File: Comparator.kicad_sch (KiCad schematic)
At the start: 15 parts, among them U501 AZV3002S-13

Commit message: fix: test point changes
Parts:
- TP501, TP502: footprint TestPoint:TestPoint_Pad_D1.5mm -> TestPoint:TestPoint_Pad_D1.0mm
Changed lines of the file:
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@@
 			)
 		)
-		(property "Footprint" "TestPoint:TestPoint_Pad_D1.5mm"
+		(property "Footprint" "TestPoint:TestPoint_Pad_D1.0mm"
 			(at 87.63 66.04 0)
 			(effects
@@
 			)
 		)
-		(property "Datasheet" "~"
+		(property "Datasheet" ""
 			(at 87.63 66.04 0)
 			(effects
@@
 			)
 		)
-		(property "Description" "test point"
+		(property "Description" ""
 			(at 92.71 66.04 0)
 			(effects
@@
 			)
 		)
-		(property "Footprint" "TestPoint:TestPoint_Pad_D1.5mm"
+		(property "Footprint" "TestPoint:TestPoint_Pad_D1.0mm"
 			(at 151.13 66.04 0)
 			(effects
@@
 			)
 		)
-		(property "Datasheet" "~"
+		(property "Datasheet" ""
 			(at 151.13 66.04 0)
 			(effects
@@
 			)
 		)
-		(property "Description" "test point"
+		(property "Description" ""
 			(at 156.21 66.04 0)
 			(effects

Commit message: fix: bom improvements & more notes
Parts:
- D501, D502: Notes (none) -> Fast switching diode, low leakage, used for diode-AND logic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
- TP501, TP502: footprint TestPoint:TestPoint_Pad_D1.0mm -> RD-Testpoints:TestPoint_Pad_D1.0mm
- TP503: footprint TestPoint:TestPoint_Pad_D1.5mm -> RD-Testpoints:TestPoint_Pad_D1.5mm
- U501: Notes (none) -> Dual comparator, low supply current, wide supply voltage ra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
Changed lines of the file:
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@@
 			)
 		)
-		(property "Footprint" "TestPoint:TestPoint_Pad_D1.0mm"
+		(property "Footprint" "RD-Testpoints:TestPoint_Pad_D1.0mm"
 			(at 87.63 66.04 0)
 			(effects
@@
 			)
 		)
-		(property "Footprint" "TestPoint:TestPoint_Pad_D1.5mm"
+		(property "Footprint" "RD-Testpoints:TestPoint_Pad_D1.5mm"
 			(at 208.28 72.39 0)
 			(effects
@@
 			)
 		)
+		(property "Notes" "Dual comparator, low supply current, wide supply voltage range, suitable for voltage threshold detection"
+			(at 130.81 66.04 0)
+			(effects
+				(font
+					(size 1.27 1.27)
+				)
+				(hide yes)
+			)
+		)
 		(pin "6"
 		)
@@
 			)
 		)
-		(property "Footprint" "TestPoint:TestPoint_Pad_D1.0mm"
+		(property "Footprint" "RD-Testpoints:TestPoint_Pad_D1.0mm"
 			(at 151.13 66.04 0)
 			(effects
@@
 			)
 		)
+		(property "Notes" "Fast switching diode, low leakage, used for diode-AND logic gating of control signals"
+			(at 195.58 85.09 0)
+			(effects
+				(font
+					(size 1.27 1.27)
+				)
+				(hide yes)
+			)
+		)
 		(pin "1"
 		)
@@
 				)
 				(justify left top)
+				(hide yes)
+			)
+		)
+		(property "Notes" "Dual comparator, low supply current, wide supply voltage range, suitable for voltage threshold detection"
+			(at 67.31 66.04 0)
+			(effects
+				(font
+					(size 1.27 1.27)
+				)
 				(hide yes)
 			)
@@
 			(at 195.58 72.39 0)
 			(effects
+				(font
+					(size 1.27 1.27)
+				)
+				(hide yes)
+			)
+		)
+		(property "Notes" "Fast switching diode, low leakage, used for diode-AND logic gating of control signals"
+			(at 195.58 72.39 0)
+			(effects

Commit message: feat: ERC/DRC checks
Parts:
- R501, R502, R503, R504, R505, R506, R507: Manufacturer (none) -> Analog Technologies
- U501: footprint Package_SO:Diodes_SO-8EP -> AZV3002S-13:Diodes_SO-8EP

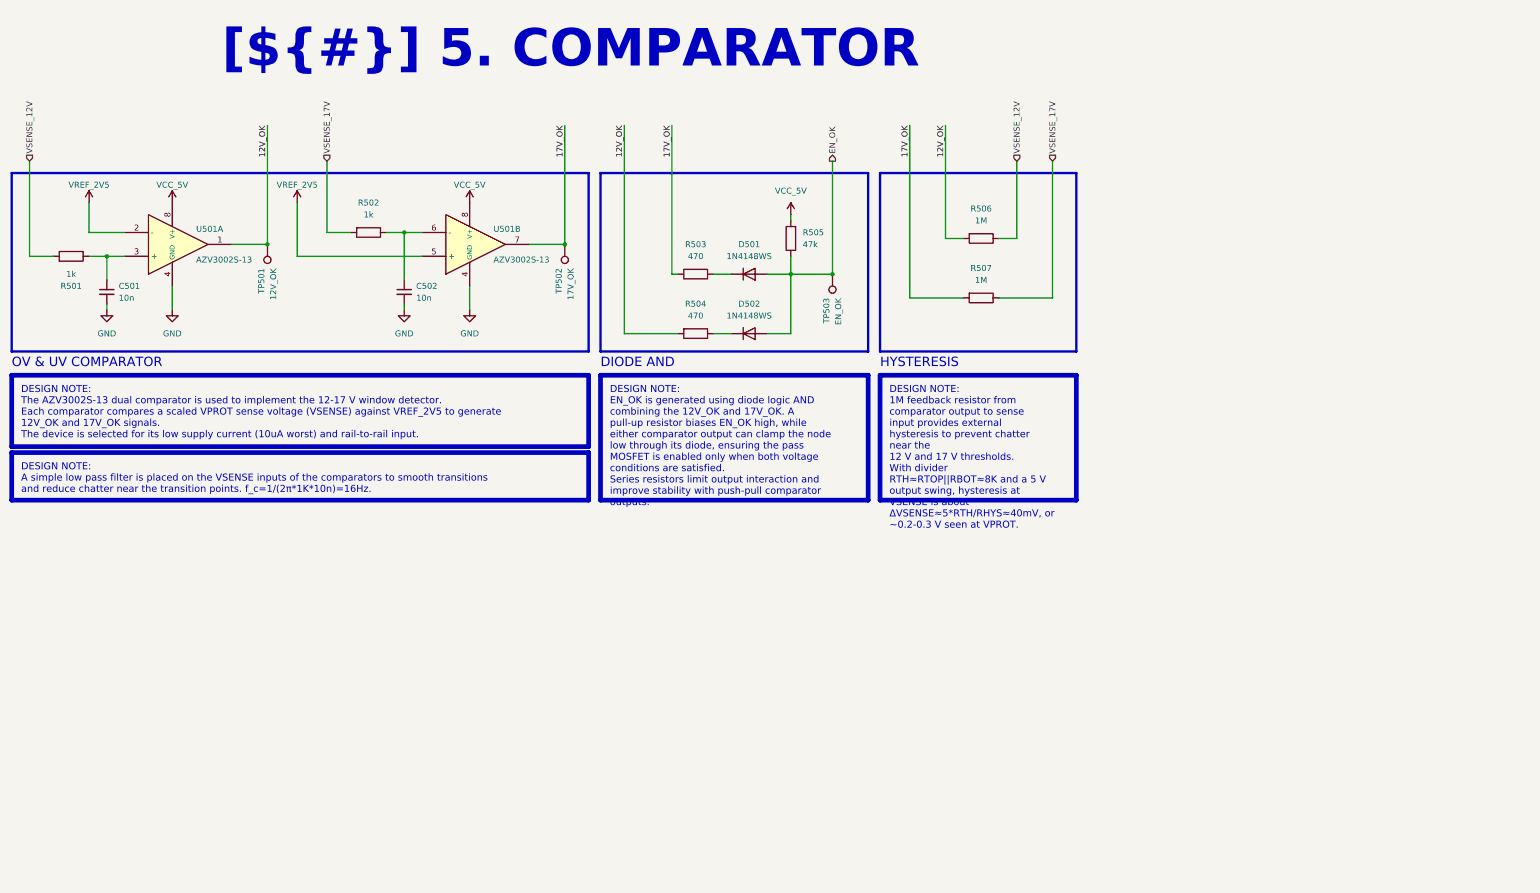
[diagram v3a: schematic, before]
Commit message: feat!: added OC protection, redesigned board from near scratch, size increase
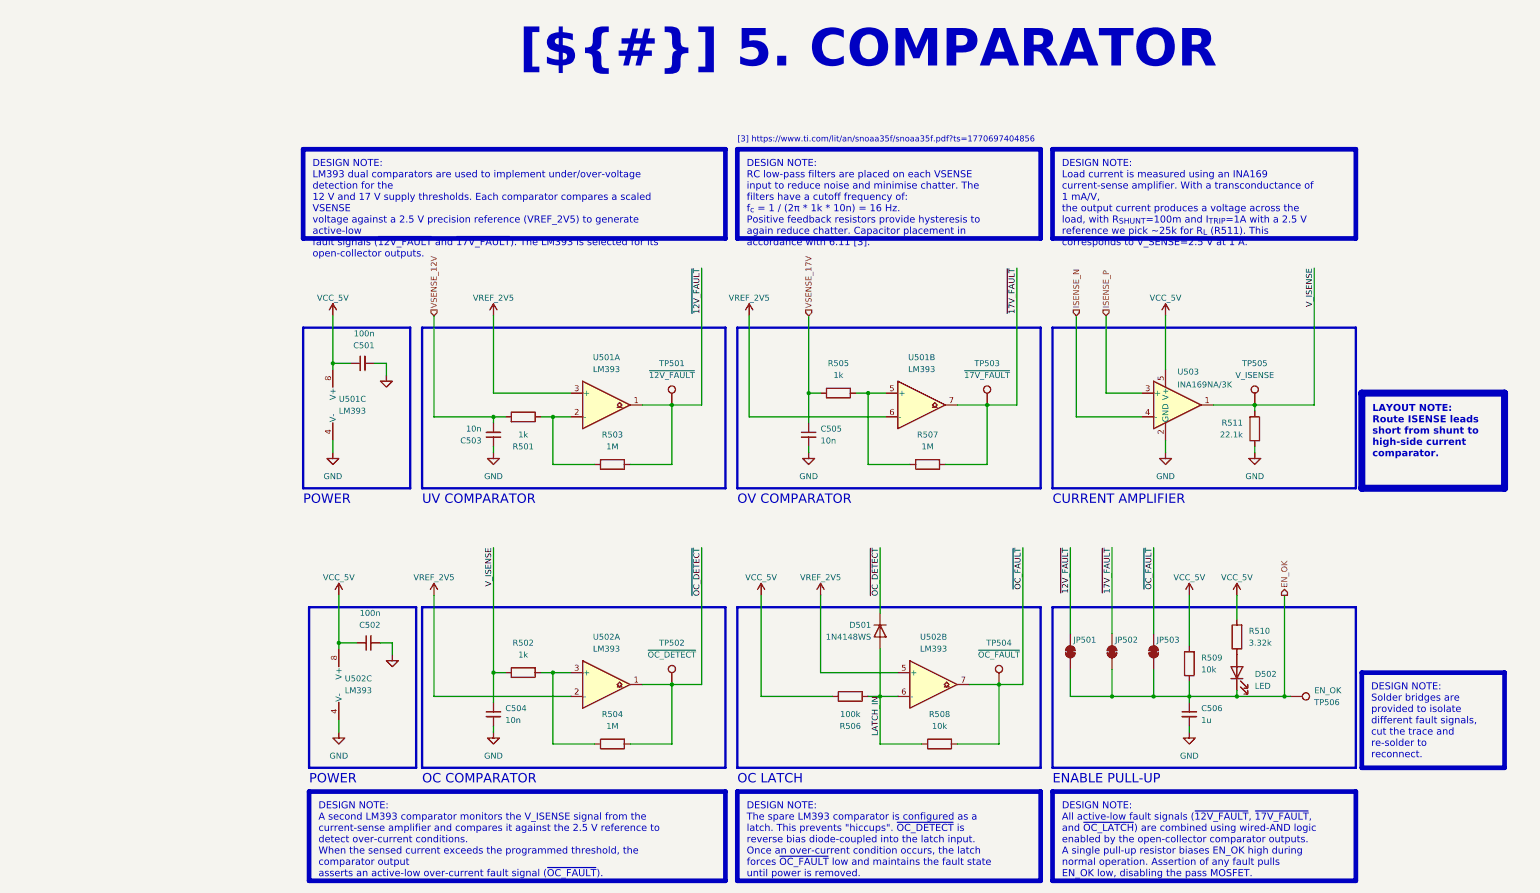
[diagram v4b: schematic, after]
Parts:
- removed D502: 1N4148WS, Diode_SMD:D_SOD-323, symbol Diode:1N4148WS
- removed R503: 470, Resistor_SMD:R_1206_3216Metric_Pad1.30x1.75mm_HandSolder, symbol Device:R
- removed U501: AZV3002S-13, AZV3002S-13:Diodes_SO-8EP, symbol AZV3002S-13:AZV3002S-13
- added C501: 100n, Capacitor_SMD:C_0603_1608Metric_Pad1.08x0.95mm_HandSolder, symbol Device:C_Small
- added C504, C505: 10n, Capacitor_SMD:C_0603_1608Metric_Pad1.08x0.95mm_HandSolder, symbol Device:C_Small
- added C506: 1u, Capacitor_SMD:C_0603_1608Metric_Pad1.08x0.95mm_HandSolder, symbol Device:C_Small
- added D502: LED, LED_SMD:LED_0805_2012Metric_Pad1.15x1.40mm_HandSolder, symbol Device:LED
- added JP501, JP502, JP503: SolderJumper_2_Bridged, Jumper:SolderJumper-2_P1.3mm_Bridged_Pad1.0x1.5mm, symbol Jumper:SolderJumper_2_Bridged
- added R505: 1k, Resistor_SMD:R_1206_3216Metric_Pad1.30x1.75mm_HandSolder, symbol Device:R
- added R506: 100k, Resistor_SMD:R_1206_3216Metric_Pad1.30x1.75mm_HandSolder, symbol Device:R
- added R508: 10k, Resistor_SMD:R_1206_3216Metric_Pad1.30x1.75mm_HandSolder, symbol Device:R
- added R510: 3.32k, Resistor_SMD:R_1206_3216Metric_Pad1.30x1.75mm_HandSolder, symbol Device:R
- added R511: 22.1k, Resistor_SMD:R_1206_3216Metric_Pad1.30x1.75mm_HandSolder, symbol Device:R
- added TP502: ~{OC_DETECT}, RD-Testpoints:TestPoint_Pad_D1.0mm, symbol Connector:TestPoint
- added TP504: ~{OC_FAULT}, RD-Testpoints:TestPoint_Pad_D1.0mm, symbol Connector:TestPoint
- added TP505: V_ISENSE, RD-Testpoints:TestPoint_Pad_D1.0mm, symbol Connector:TestPoint
- added U501, U502: LM393, Package_SO:SOIC-8_3.9x4.9mm_P1.27mm, symbol Comparator:LM393
- added U503: INA169NA/3K, Package_TO_SOT_SMD:SOT-23-5, symbol Amplifier_Current:INA169
- C502: value 10n -> 100n; MPN C1608X7R1H103KT -> C1608X7R1C104KT; Voltage_Rating 50V -> 16V
- R504: value 470 -> 1M
- R509: renamed from R505; value 47k -> 10k
- TP501: value 12V_OK -> ~{12V_FAULT}
- TP503: renamed from TP502; value 17V_OK -> ~{17V_FAULT}
- TP506: renamed from TP503; footprint RD-Testpoints:TestPoint_Pad_D1.5mm -> RD-Testpoints:TestPoint_Pad_D1.0mm
- renumbered C501 to C503, R506 to R503
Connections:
- net EN_OK: now also C506.1, D502.1 (K), JP501.1 (A), JP502.1 (A), JP503.1 (A); no longer D501.2 (A)
- net GND: now also C503.1, C501.2, C504.2, C505.2, C506.2, R511.1, U501.4 (V-), U502.4 (V-), U503.2 (GND); no longer C503.2
- net VCC_5V: now also C502.1, C501.1, R506.2, R510.2, U501.8 (V+), U502.8 (V+), U503.5 (V+)
- net VREF_2V5: now also U501.3 (+), U501.6 (-), U502.2 (-), U502.5 (+)
- net VSENSE_12V: now also C503.2; no longer R503.1
- net VSENSE_17V: now also C505.1, R505.1; no longer R502.2, R507.1
- net V_ISENSE: now reaches R502.1
- net V_ISENSE: now also C504.1, R511.2, TP505.1, U503.1; no longer C502.1
- net at R501.1: now also R503.1, U501.2 (-); no longer C503.1
- net at R504.1: now also R502.2, U502.3 (+)
- net ~{OC_DETECT}: now reaches D501.1 (K)
- net ~{OC_DETECT}: now also R504.2, TP502.1, U502.1
- net 12V_OK renamed ~{12V_FAULT}
- net ~{12V_FAULT}: now also JP501.2 (B), U501.1; no longer R504.2
- net 17V_OK renamed ~{17V_FAULT}
- net ~{17V_FAULT}: now also JP502.2 (B), U501.7
- new net: R505.2, R507.1, U501.5 (+)
- new net: D502.2 (A), R510.1
- new net ISENSE_N: U503.4 (-)
- new net ISENSE_P: U503.3 (+)
- new net LATCH_IN: D501.2 (A), R506.1, R508.1, U502.6 (-)
- new net ~{OC_FAULT}: JP503.2 (B), R508.2, TP504.1, U502.7
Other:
- note added: "CURRENT AMPLIFIER"
- note added: "ENABLE PULL-UP"
- note added: "OC COMPARATOR"
- note added: "OC LATCH"
- note added: "OV COMPARATOR"
- note added: "POWER"
- note added: "UV COMPARATOR"
- note added: "[3] https://www.ti.com/lit/an/snoaa35f/snoaa35f.pdf?ts=1770697404856"
- note removed: "DIODE AND"
- note removed: "HYSTERESIS"
- note removed: "OV & UV COMPARATOR"
- moved on the sheet: C503, R501, R503, R509, TP501, TP503, TP506

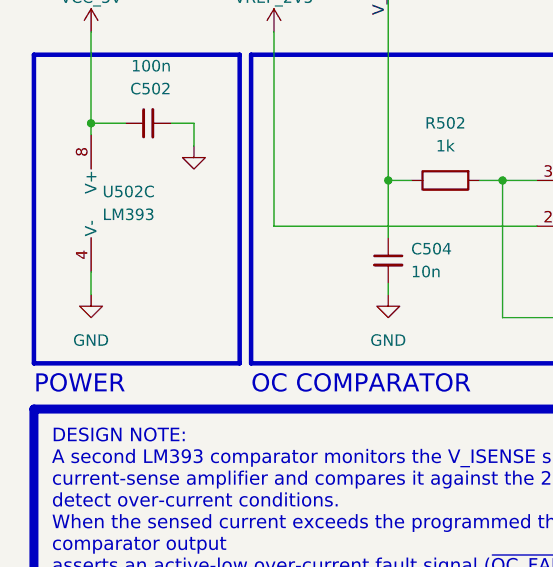
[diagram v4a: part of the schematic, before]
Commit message: fix: fab layer clean up and bom additions
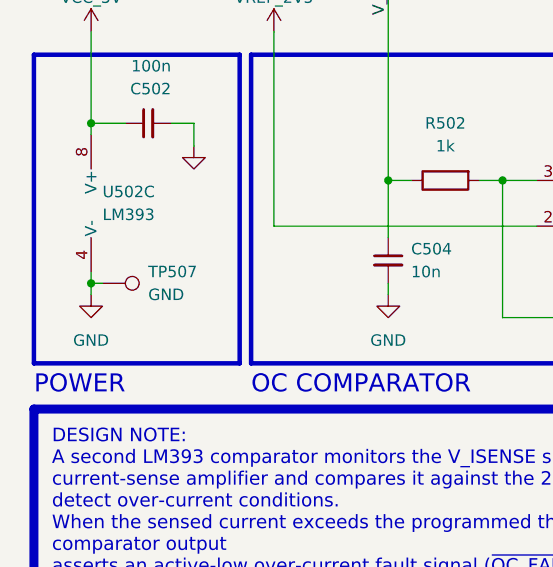
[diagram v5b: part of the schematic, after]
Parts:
- added TP507: GND, RD-Testpoints:TestPoint_THTPad_1.5x1.5mm_Drill0.7mm, symbol Connector:TestPoint
- U502: MPN (none) -> LM393ADT; Manufacturer (none) -> Texas Instruments; Notes (none) -> Open-collector output required, >5V tolerant inputs.
- U503: Notes (none) -> Transconductance of 1mA/V
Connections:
- net GND: now also TP507.1
